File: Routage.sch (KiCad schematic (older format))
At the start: 52 parts, among them J2 Conn_01x02, J3 Conn_01x03, Q1 2N2907, Q10 TIP32, Q11 BD138, Q12 TIP31, Q13 2N2222, Q2 2N2907, Q3 2N2907, Q4 2N2222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

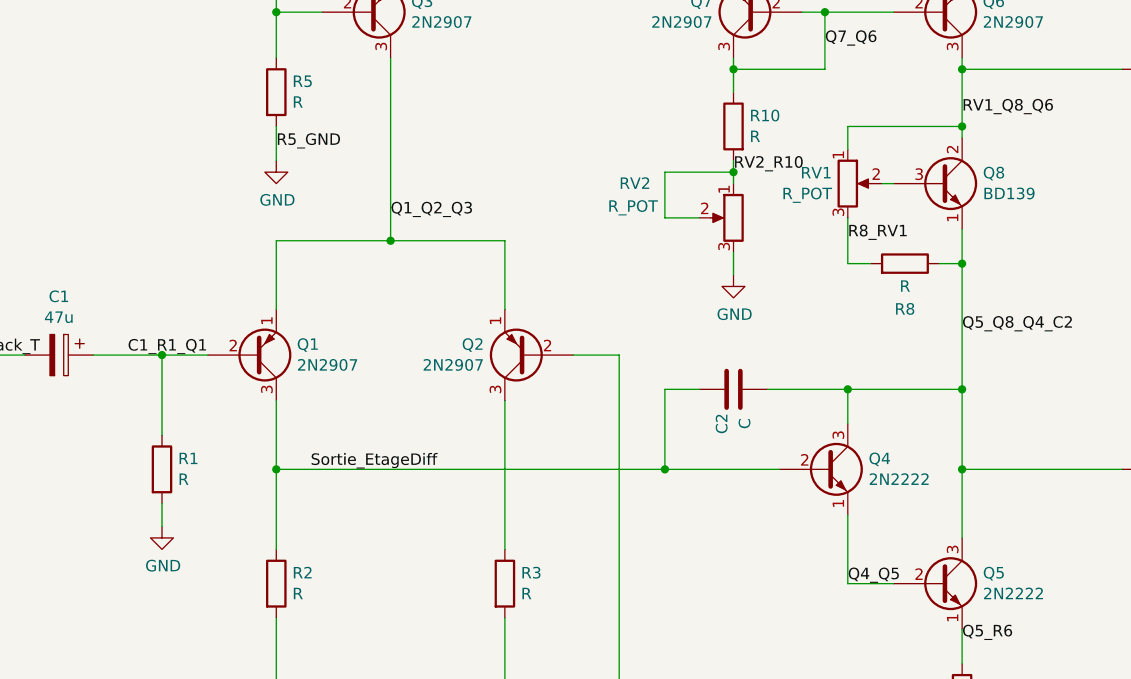
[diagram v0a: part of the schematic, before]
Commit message: routage modifie
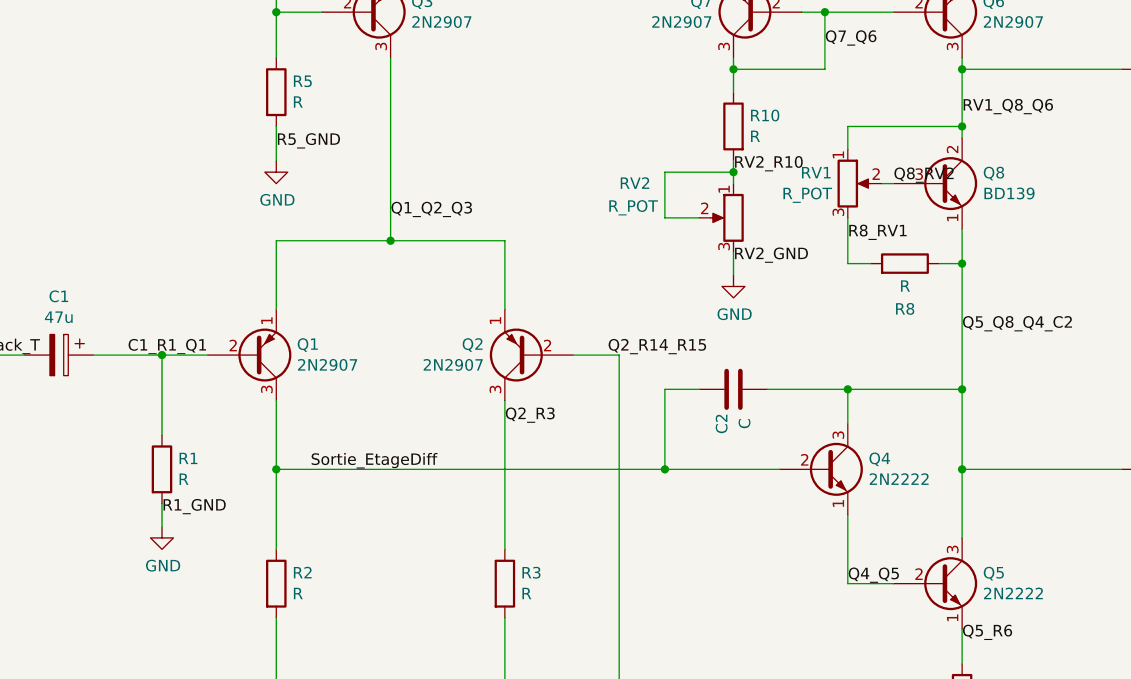
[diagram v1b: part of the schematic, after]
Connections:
- net Q2_R3: now reaches Q2.3 (C), R3.1
- net Q2_R14_R15: now reaches Q2.2 (B), R14.2, R15.1
- net Q8_RV2: now reaches Q8.3 (B), RV1.2
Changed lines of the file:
@@
 Text Label 9050 3750 0    50   ~ 0
 Relay_Q13
+Text Label 1900 4100 0    50   ~ 0
+R1_GND
+Text Label 3400 3700 0    50   ~ 0
+Q2_R3
+Text Label 3850 3400 0    50   ~ 0
+Q2_R14_R15
+Text Label 4400 3000 0    50   ~ 0
+RV2_GND
+Text Label 5100 2650 0    50   ~ 0
+Q8_RV2
 $EndSCHEMATC

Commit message: Routage modifie 2
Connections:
- net GND: now also J2.1 (Pin_1); no longer J2.2 (Pin_2)
- net Relay_J2: now also J2.2 (Pin_2); no longer J2.1 (Pin_1)
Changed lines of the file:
@@
 L Connector_Generic:Conn_01x02 J2
 U 1 1 5E82A477
-P 10650 3000
-F 0 "J2" H 10730 2992 50  0000 L CNN
-F 1 "Conn_01x02" H 10730 2901 50  0000 L CNN
-F 2 "CmpAmpliAudio:PhoenixContact_MSTBVA_2,5_2-G-5,08_1x02_P5.08mm_Vertical" H 10650 3000 50  0001 C CNN
-F 3 "~" H 10650 3000 50  0001 C CNN
-	1    10650 3000
-	1    0    0    -1
+P 10650 3100
+F 0 "J2" H 10730 3092 50  0000 L CNN
+F 1 "Conn_01x02" H 10730 3001 50  0000 L CNN
+F 2 "CmpAmpliAudio:PhoenixContact_MSTBVA_2,5_2-G-5,08_1x02_P5.08mm_Vertical" H 10650 3100 50  0001 C CNN
+F 3 "~" H 10650 3100 50  0001 C CNN
+	1    10650 3100
+	1    0    0    1
 $EndComp
 Wire Wire Line
